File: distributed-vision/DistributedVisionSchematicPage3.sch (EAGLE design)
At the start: 57 parts, among them Q1 AP2331SA-7, U1 TPS70625DBVR, U2 LM26420XMH

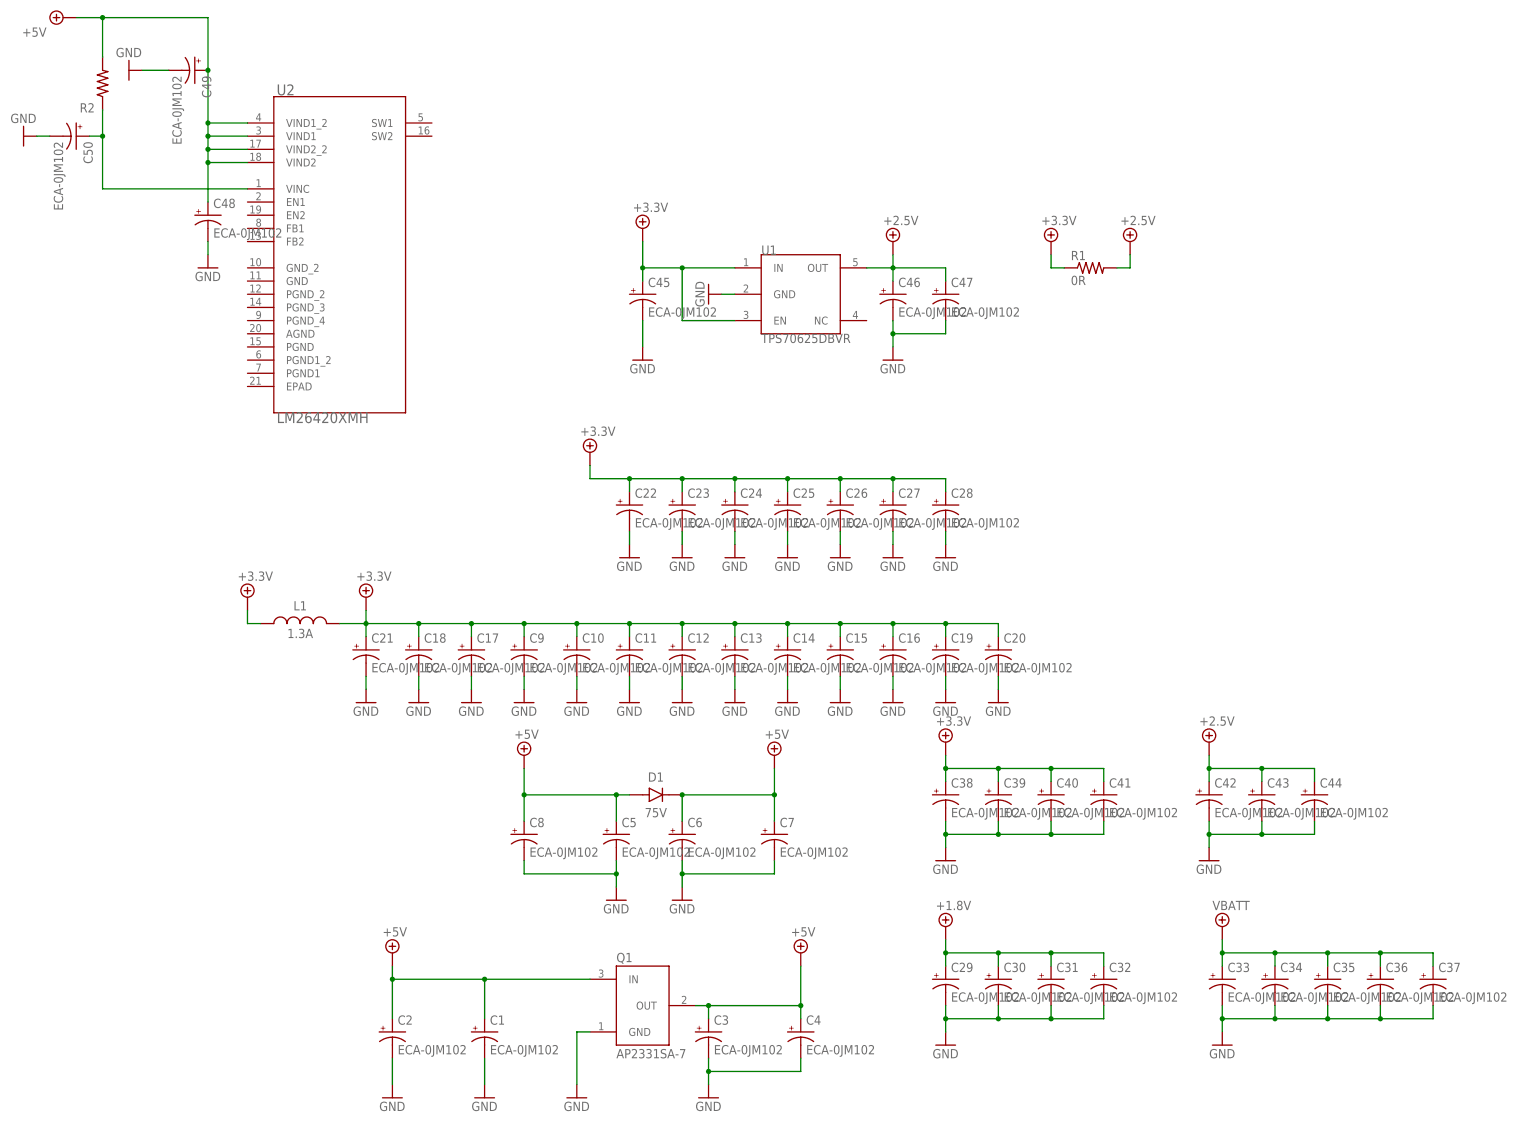
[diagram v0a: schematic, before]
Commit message: Updated Capacitors/Resistors
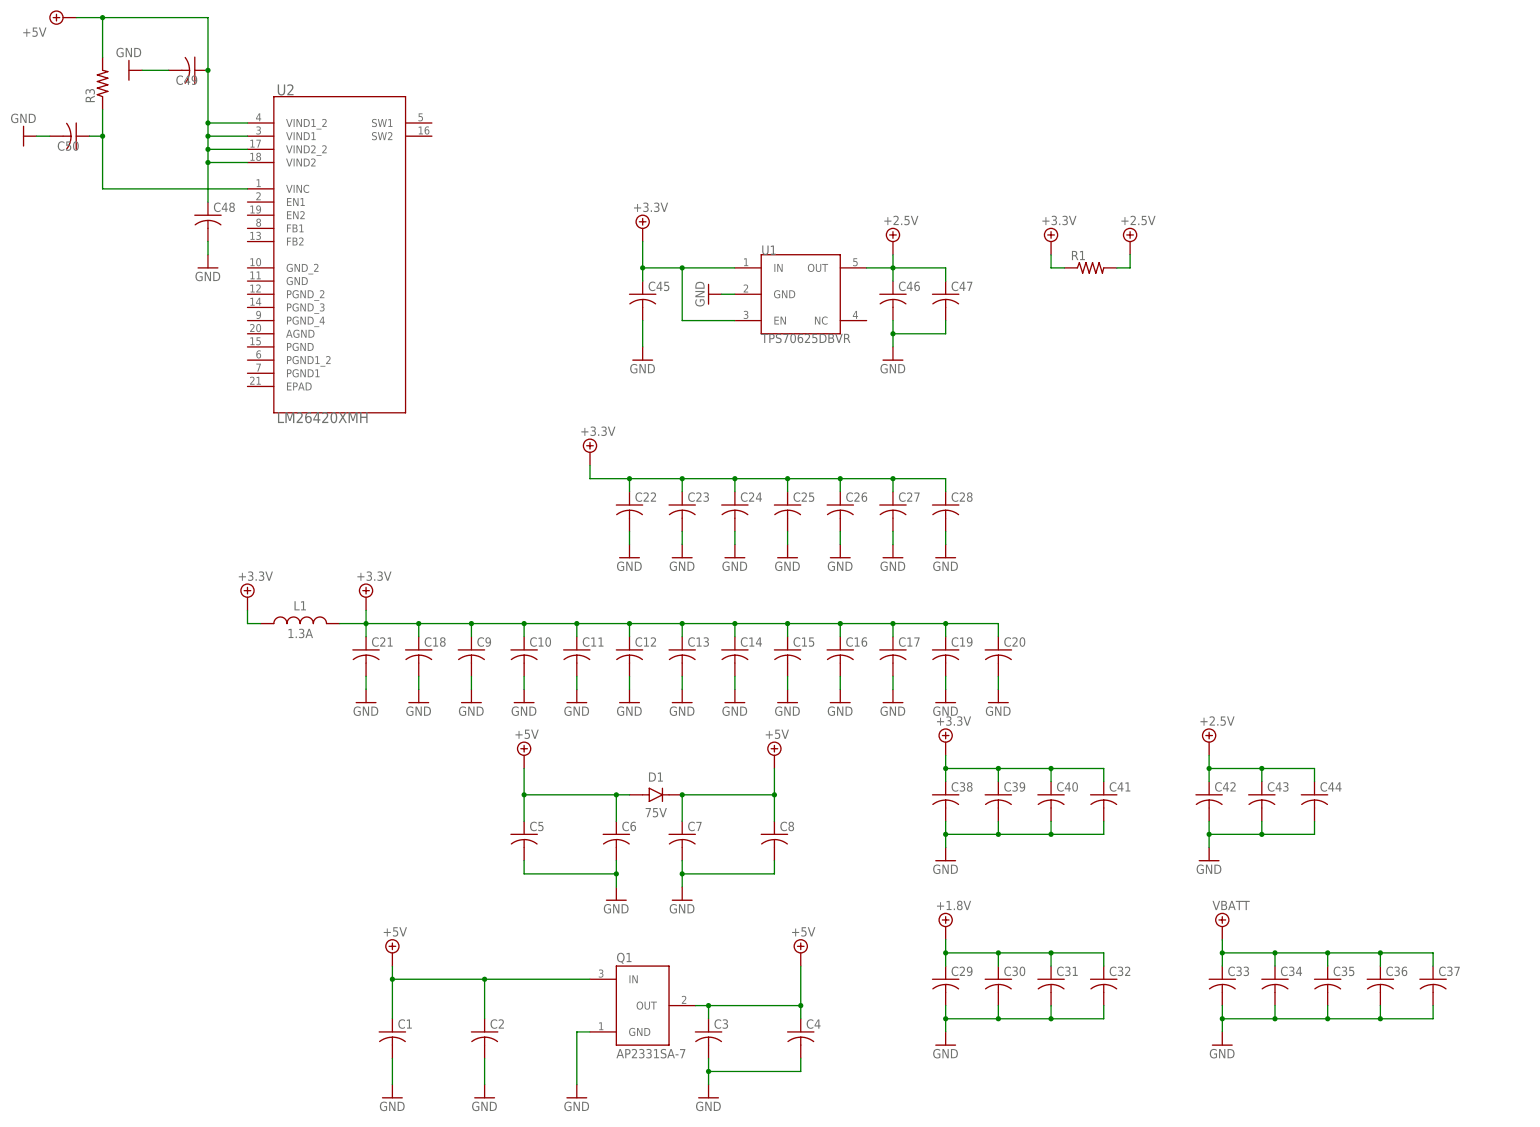
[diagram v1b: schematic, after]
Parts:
- removed R2: (no value), RoboJackets-Resistors:ERJ-L06KF50MV
- added R3: (no value), rcl:R-US_R0603
- C1, C10, C11, C12, C13, C14, C15, C16, C17, C18, C19, C2, C20, C21, C22, C23, C24, C25, C26, C27, C28, C29, C3, C30, C31, C32, C33, C34, C35, C36, C37, C38, C39, C4, C40, C41, C42, C43, C44, C45, C46, C47, C48, C49, C5, C50, C6, C7, C8, C9: value ECA-0JM102 -> (none); device RoboJackets-Capacitors:ECA-0JM102 -> rcl:C-USC0603
- R1: value 0R -> (none); device RoboJackets-Resistors:ERJ-L06KF50MV -> rcl:R-US_R0603
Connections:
- net +1.8V: now also C29.1, C30.1, C31.1, C32.1; no longer C29.+, C30.+, C31.+, C32.+
- net +2.5V: now also C42.1, C43.1, C44.1, C46.1, C47.1, R1.2; no longer C42.+, C43.+, C44.+, C46.+, C47.+, R1.PIN2
- net +3.3V: now also C10.1, C11.1, C12.1, C13.1, C14.1, C15.1, C16.1, C17.1, C18.1, C19.1, C20.1, C21.1, C22.1, C23.1, C24.1, C25.1, C26.1, C27.1, C28.1, C38.1, C39.1, C40.1, C41.1, C45.1, C9.1, R1.1; no longer C10.+, C11.+, C12.+, C13.+, C14.+, C15.+, C16.+, C17.+, C18.+, C19.+, C20.+, C21.+, C22.+, C23.+, C24.+, C25.+, C26.+, C27.+, C28.+, C38.+, C39.+, C40.+, C41.+, C45.+, C9.+, R1.PIN1
- net +5V: now also C1.1, C2.1, C3.1, C4.1, C48.1, C49.1, C5.1, C6.1, C7.1, C8.1, R3.2; no longer C1.+, C2.+, C3.+, C4.+, C48.+, C49.+, C5.+, C6.+, C7.+, C8.+, R2.PIN2
- net GND: now also C1.2, C10.2, C11.2, C12.2, C13.2, C14.2, C15.2, C16.2, C17.2, C18.2, C19.2, C2.2, C20.2, C21.2, C22.2, C23.2, C24.2, C25.2, C26.2, C27.2, C28.2, C29.2, C3.2, C30.2, C31.2, C32.2, C33.2, C34.2, C35.2, C36.2, C37.2, C38.2, C39.2, C4.2, C40.2, C41.2, C42.2, C43.2, C44.2, C45.2, C46.2, C47.2, C48.2, C49.2, C5.2, C50.2, C6.2, C7.2, C8.2, C9.2; no longer C1.-, C10.-, C11.-, C12.-, C13.-, C14.-, C15.-, C16.-, C17.-, C18.-, C19.-, C2.-, C20.-, C21.-, C22.-, C23.-, C24.-, C25.-, C26.-, C27.-, C28.-, C29.-, C3.-, C30.-, C31.-, C32.-, C33.-, C34.-, C35.-, C36.-, C37.-, C38.-, C39.-, C4.-, C40.-, C41.-, C42.-, C43.-, C44.-, C45.-, C46.-, C47.-, C48.-, C49.-, C5.-, C50.-, C6.-, C7.-, C8.-, C9.-
- net N$5: now also C50.1, R3.1; no longer C50.+, R2.PIN1
- net VBATT: now also C33.1, C34.1, C35.1, C36.1, C37.1; no longer C33.+, C34.+, C35.+, C36.+, C37.+
